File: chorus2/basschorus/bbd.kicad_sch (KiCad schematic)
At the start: 16 parts, among them J1 AVR-ISP-6, U2 ATtiny25-20S

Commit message: code implementation
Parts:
- removed C13, C14: 1u, symbol Device:C_Polarized_US
- removed R5: 10k, symbol Device:R
- added C30: 100n, symbol Device:C
- added Q1: 2N3904, Package_TO_SOT_THT:TO-92_Inline, symbol Transistor_BJT:2N3904
- added R35, R36: 180, symbol Device:R
- added R37: 3.3k, symbol Device:R
- added R38: 2.2k, symbol Device:R
- RV1: value B100K_DEPTH -> B100K_WIDTH
- RV2: value B100K_WIDTH -> B100K_DEPTH
- renumbered C8 to C12, C10 to C13, C2 to C14, C3 to C15, C6 to C9, J1 to J4, R4 to R16, R3 to R17, U2 to U7, U1 to U8
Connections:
- net +5V: now also RV1.1, R36.1, R37.1; no longer RV1.3
- net GND: now also RV1.3, R35.2, R38.2; no longer RV1.1
- new net: C30.2, Q1.2 (B), R37.2, R38.1
- new net: Q1.1 (E), R35.1
- new net: Q1.3 (C), R36.2
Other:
- note added: "3.2V -> (5-3.2)/10mA => Re=180 Gain ~= 1 => Rc=Re"
- note added: "DC offset TODO: an opamp would be worthwhile here... should be possible to add DC offset to AA filter (based on datasheet)"
- note added: "NOTE: inverted pot (clockwise = more freq = less period)"
- moved on the sheet: RV1

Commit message: fix logic
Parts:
- removed C30: 100n, symbol Device:C
- removed Q1: 2N3904, Package_TO_SOT_THT:TO-92_Inline, symbol Transistor_BJT:2N3904
- removed R35, R36: 180, symbol Device:R
- removed R37: 3.3k, symbol Device:R
- removed R38: 2.2k, symbol Device:R
- added D2: LED, symbol Device:LED
- added R15: 1k, symbol Device:R
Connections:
- net +5V: now also R15.1
- net at J4.3 (SCK), U7.7 (PB2): now also D2.1 (K); no longer RV1.2
- net at U7.2 (XTAL1/PB3): now also RV2.2
- net at U7.3 (XTAL2/PB4): now also RV1.2; no longer RV2.2
- new net: D2.2 (A), R15.2
- no-connect marks 1 -> 0
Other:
- note removed: "3.2V -> (5-3.2)/10mA => Re=180 Gain ~= 1 => Rc=Re"
- moved on the sheet: RV1, RV2

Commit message: transfer function
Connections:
- net +5V: now also RV1.3; no longer RV1.1
- net GND: now also RV1.1; no longer RV1.3
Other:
- note removed: "NOTE: inverted pot (clockwise = more freq = less period)"
- moved on the sheet: RV1
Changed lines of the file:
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@@
 		)
 	)
-	(text "NOTE: inverted pot\n(clockwise = more freq = less period)"
-		(exclude_from_sim no)
-		(at 172.72 156.21 0)
-		(effects
-			(font
-				(size 1.27 1.27)
-			)
-		)
-	)
 	(junction
 		(at 162.56 72.39)
@@
 	(symbol
 		(lib_id "Device:R_Potentiometer")
-		(at 157.48 147.32 0)
-		(mirror y)
+		(at 157.48 147.32 180)
 		(unit 1)
 		(exclude_from_sim no)
@@
 		(dnp no)
 		(property "Reference" "RV1"
-			(at 160.02 148.5901 0)
+			(at 160.02 146.0499 0)
 			(effects
 				(font
@@
 		)
 		(property "Value" "B100K_WIDTH"
-			(at 160.02 146.0501 0)
+			(at 160.02 148.5899 0)
 			(effects
 				(font

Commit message: update filters
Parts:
- renumbered C9 to C11, R15 to R16, R16 to R17, R17 to R18, RV2 to RV1, RV1 to RV2
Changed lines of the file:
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@@
 		(dnp no)
 		(fields_autoplaced yes)
-		(property "Reference" "#PWR042"
+		(property "Reference" "#PWR047"
 			(at 259.08 73.66 0)
 			(effects
@@
 			(project "basschorus"
 				(path "/7f3b4bac-3b2a-4af0-92ae-ccc3fcedc393/6358d57b-3820-48b6-8dc6-10ef393466f2"
-					(reference "#PWR042")
+					(reference "#PWR047")
 					(unit 1)
 				)
@@
 		(dnp no)
 		(fields_autoplaced yes)
-		(property "Reference" "#PWR023"
+		(property "Reference" "#PWR030"
 			(at 57.15 68.58 0)
 			(effects
@@
 			(project "basschorus"
 				(path "/7f3b4bac-3b2a-4af0-92ae-ccc3fcedc393/6358d57b-3820-48b6-8dc6-10ef393466f2"
-					(reference "#PWR023")
+					(reference "#PWR030")
 					(unit 1)
 				)
@@
 		(dnp no)
 		(fields_autoplaced yes)
-		(property "Reference" "#PWR041"
+		(property "Reference" "#PWR046"
 			(at 242.57 92.71 0)
 			(effects
@@
 			(project "basschorus"
 				(path "/7f3b4bac-3b2a-4af0-92ae-ccc3fcedc393/6358d57b-3820-48b6-8dc6-10ef393466f2"
-					(reference "#PWR041")
+					(reference "#PWR046")
 					(unit 1)
 				)
@@
 		(dnp no)
 		(fields_autoplaced yes)
-		(property "Reference" "#PWR035"
+		(property "Reference" "#PWR040"
 			(at 157.48 160.02 0)
 			(effects
@@
 			(project "basschorus"
 				(path "/7f3b4bac-3b2a-4af0-92ae-ccc3fcedc393/6358d57b-3820-48b6-8dc6-10ef393466f2"
-					(reference "#PWR035")
+					(reference "#PWR040")
 					(unit 1)
 				)
@@
 		(dnp no)
 		(fields_autoplaced yes)
-		(property "Reference" "R15"
+		(property "Reference" "R16"
 			(at 120.65 39.3699 0)
 			(effects
@@
 			(project ""
 				(path "/7f3b4bac-3b2a-4af0-92ae-ccc3fcedc393/6358d57b-3820-48b6-8dc6-10ef393466f2"
-					(reference "R15")
+					(reference "R16")
 					(unit 1)
 				)
@@
 		(dnp no)
 		(fields_autoplaced yes)
-		(property "Reference" "#PWR026"
+		(property "Reference" "#PWR033"
 			(at 86.36 142.24 0)
 			(effects
@@
 			(project "basschorus"
 				(path "/7f3b4bac-3b2a-4af0-92ae-ccc3fcedc393/6358d57b-3820-48b6-8dc6-10ef393466f2"
-					(reference "#PWR026")
+					(reference "#PWR033")
 					(unit 1)
 				)
@@
 		(dnp no)
 		(fields_autoplaced yes)
-		(property "Reference" "#PWR037"
+		(property "Reference" "#PWR042"
 			(at 173.99 93.98 0)
 			(effects
@@
 			(project "basschorus"
 				(path "/7f3b4bac-3b2a-4af0-92ae-ccc3fcedc393/6358d57b-3820-48b6-8dc6-10ef393466f2"
-					(reference "#PWR037")
+					(reference "#PWR042")
 					(unit 1)
 				)
@@
 		(dnp no)
 		(fields_autoplaced yes)
-		(property "Reference" "#PWR024"
+		(property "Reference" "#PWR031"
 			(at 57.15 83.82 0)
 			(effects
@@
 			(project "basschorus"
 				(path "/7f3b4bac-3b2a-4af0-92ae-ccc3fcedc393/6358d57b-3820-48b6-8dc6-10ef393466f2"
-					(reference "#PWR024")
+					(reference "#PWR031")
 					(unit 1)
 				)
@@
 		(dnp no)
 		(fields_autoplaced yes)
-		(property "Reference" "#PWR027"
+		(property "Reference" "#PWR034"
 			(at 92.71 59.69 0)
 			(effects
@@
 			(project "basschorus"
 				(path "/7f3b4bac-3b2a-4af0-92ae-ccc3fcedc393/6358d57b-3820-48b6-8dc6-10ef393466f2"
-					(reference "#PWR027")
+					(reference "#PWR034")
 					(unit 1)
 				)
@@
 		(dnp no)
 		(fields_autoplaced yes)
-		(property "Reference" "R17"
+		(property "Reference" "R18"
 			(at 245.11 77.4699 0)
 			(effects
@@
 			(project "basschorus"
 				(path "/7f3b4bac-3b2a-4af0-92ae-ccc3fcedc393/6358d57b-3820-48b6-8dc6-10ef393466f2"
-					(reference "R17")
+					(reference "R18")
 					(unit 1)
 				)
@@
 		(dnp no)
 		(fields_autoplaced yes)
-		(property "Reference" "#PWR038"
+		(property "Reference" "#PWR043"
 			(at 181.61 93.98 0)
 			(effects
@@
 			(project "basschorus"
 				(path "/7f3b4bac-3b2a-4af0-92ae-ccc3fcedc393/6358d57b-3820-48b6-8dc6-10ef393466f2"
-					(reference "#PWR038")
+					(reference "#PWR043")
 					(unit 1)
 				)
@@
 		(dnp no)
 		(fields_autoplaced yes)
-		(property "Reference" "#PWR029"
+		(property "Reference" "#PWR036"
 			(at 118.11 38.1 0)
 			(effects
@@
 			(project "basschorus"
 				(path "/7f3b4bac-3b2a-4af0-92ae-ccc3fcedc393/6358d57b-3820-48b6-8dc6-10ef393466f2"
-					(reference "#PWR029")
+					(reference "#PWR036")
 					(unit 1)
 				)
@@
 		(dnp no)
 		(fields_autoplaced yes)
-		(property "Reference" "#PWR040"
+		(property "Reference" "#PWR045"
 			(at 204.47 95.25 0)
 			(effects
@@
 			(project "basschorus"
 				(path "/7f3b4bac-3b2a-4af0-92ae-ccc3fcedc393/6358d57b-3820-48b6-8dc6-10ef393466f2"
-					(reference "#PWR040")
+					(reference "#PWR045")
 					(unit 1)
 				)
@@
 		(dnp no)
 		(fields_autoplaced yes)
-		(property "Reference" "#PWR039"
+		(property "Reference" "#PWR044"
 			(at 204.47 62.23 0)
 			(effects
@@
 			(project "basschorus"
 				(path "/7f3b4bac-3b2a-4af0-92ae-ccc3fcedc393/6358d57b-3820-48b6-8dc6-10ef393466f2"
-					(reference "#PWR039")
+					(reference "#PWR044")
 					(unit 1)
 				)
@@
 		(on_board yes)
 		(dnp no)
-		(property "Reference" "RV1"
+		(property "Reference" "RV2"
 			(at 160.02 146.0499 0)
 			(effects
@@
 			(project "basschorus"
 				(path "/7f3b4bac-3b2a-4af0-92ae-ccc3fcedc393/6358d57b-3820-48b6-8dc6-10ef393466f2"
-					(reference "RV1")
+					(reference "RV2")
 					(unit 1)
 				)
@@
 		(dnp no)
 		(fields_autoplaced yes)
-		(property "Reference" "#PWR036"
+		(property "Reference" "#PWR041"
 			(at 162.56 91.44 0)
 			(effects
@@
 			(project "basschorus"
 				(path "/7f3b4bac-3b2a-4af0-92ae-ccc3fcedc393/6358d57b-3820-48b6-8dc6-10ef393466f2"
-					(reference "#PWR036")
+					(reference "#PWR041")
 					(unit 1)
 				)
@@
 		(dnp no)
 		(fields_autoplaced yes)
-		(property "Reference" "C9"
+		(property "Reference" "C11"
 			(at 60.96 69.8499 0)
 			(effects
@@
 			(project "basschorus"
 				(path "/7f3b4bac-3b2a-4af0-92ae-ccc3fcedc393/6358d57b-3820-48b6-8dc6-10ef393466f2"
-					(reference "C9")
+					(reference "C11")
 					(unit 1)
 				)
@@
 		(dnp no)
 		(fields_autoplaced yes)
-		(property "Reference" "#PWR025"
+		(property "Reference" "#PWR032"
 			(at 86.36 110.49 0)
 			(effects
@@
 			(project "basschorus"
 				(path "/7f3b4bac-3b2a-4af0-92ae-ccc3fcedc393/6358d57b-3820-48b6-8dc6-10ef393466f2"
-					(reference "#PWR025")
+					(reference "#PWR032")
 					(unit 1)
 				)
@@
 		(dnp no)
 		(fields_autoplaced yes)
-		(property "Reference" "R16"
+		(property "Reference" "R17"
 			(at 156.21 66.04 90)
 			(effects
@@
 			(project "basschorus"
 				(path "/7f3b4bac-3b2a-4af0-92ae-ccc3fcedc393/6358d57b-3820-48b6-8dc6-10ef393466f2"
-					(reference "R16")
+					(reference "R17")
 					(unit 1)
 				)
@@
 		(dnp no)
 		(fields_autoplaced yes)
-		(property "Reference" "#PWR034"
+		(property "Reference" "#PWR039"
 			(at 157.48 144.78 0)
 			(effects
@@
 			(project "basschorus"
 				(path "/7f3b4bac-3b2a-4af0-92ae-ccc3fcedc393/6358d57b-3820-48b6-8dc6-10ef393466f2"
-					(reference "#PWR034")
+					(reference "#PWR039")
 					(unit 1)
 				)
@@
 		(dnp no)
 		(fields_autoplaced yes)
-		(property "Reference" "#PWR043"
+		(property "Reference" "#PWR048"
 			(at 259.08 88.9 0)
 			(effects
@@
 			(project "basschorus"
 				(path "/7f3b4bac-3b2a-4af0-92ae-ccc3fcedc393/6358d57b-3820-48b6-8dc6-10ef393466f2"
-					(reference "#PWR043")
+					(reference "#PWR048")
 					(unit 1)
 				)
@@
 		(on_board yes)
 		(dnp no)
-		(property "Reference" "RV2"
+		(property "Reference" "RV1"
 			(at 149.86 121.9199 0)
 			(effects
@@
 			(project "basschorus"
 				(path "/7f3b4bac-3b2a-4af0-92ae-ccc3fcedc393/6358d57b-3820-48b6-8dc6-10ef393466f2"
-					(reference "RV2")
+					(reference "RV1")
 					(unit 1)
 				)
@@
 		(dnp no)
 		(fields_autoplaced yes)
-		(property "Reference" "#PWR031"
+		(property "Reference" "#PWR037"
 			(at 147.32 120.65 0)
 			(effects
@@
 			(project "basschorus"
 				(path "/7f3b4bac-3b2a-4af0-92ae-ccc3fcedc393/6358d57b-3820-48b6-8dc6-10ef393466f2"
-					(reference "#PWR031")
+					(reference "#PWR037")
 					(unit 1)
 				)
@@
 		(dnp no)
 		(fields_autoplaced yes)
-		(property "Reference" "#PWR028"
+		(property "Reference" "#PWR035"
 			(at 92.71 100.33 0)
 			(effects
@@
 			(project "basschorus"
 				(path "/7f3b4bac-3b2a-4af0-92ae-ccc3fcedc393/6358d57b-3820-48b6-8dc6-10ef393466f2"
-					(reference "#PWR028")
+					(reference "#PWR035")
 					(unit 1)
 				)
@@
 		(dnp no)
 		(fields_autoplaced yes)
-		(property "Reference" "#PWR032"
+		(property "Reference" "#PWR038"
 			(at 147.32 135.89 0)
 			(effects
@@
 			(project "basschorus"
 				(path "/7f3b4bac-3b2a-4af0-92ae-ccc3fcedc393/6358d57b-3820-48b6-8dc6-10ef393466f2"
-					(reference "#PWR032")
-					(unit 1)
-				)
+					(reference "#PWR038")
+					(unit 1)
+				)

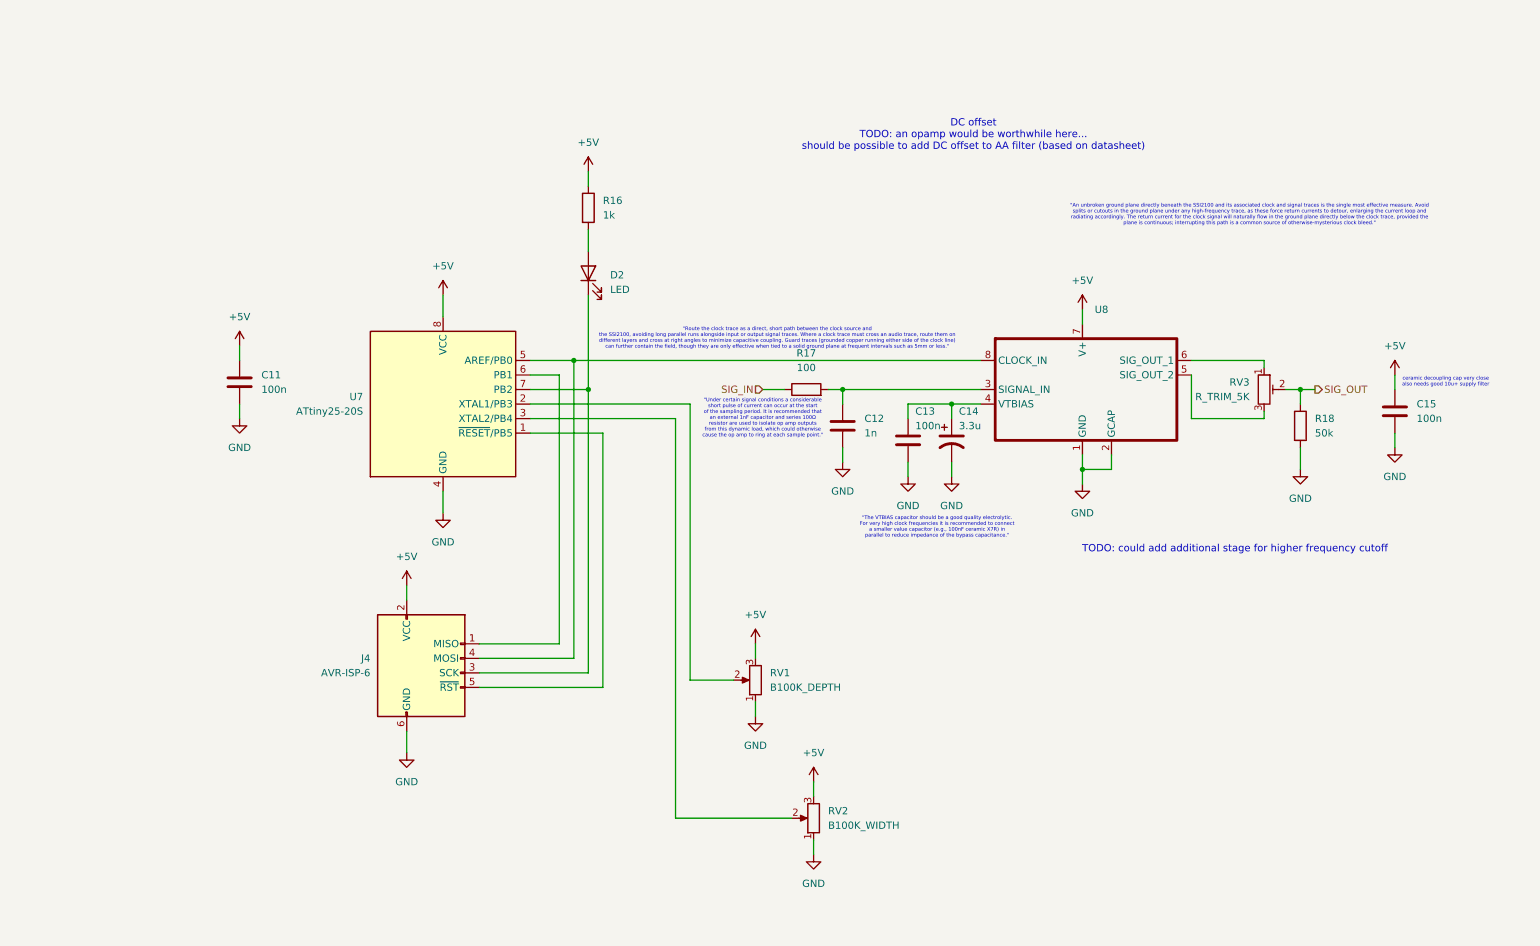
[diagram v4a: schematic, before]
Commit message: update designs based on new calculations
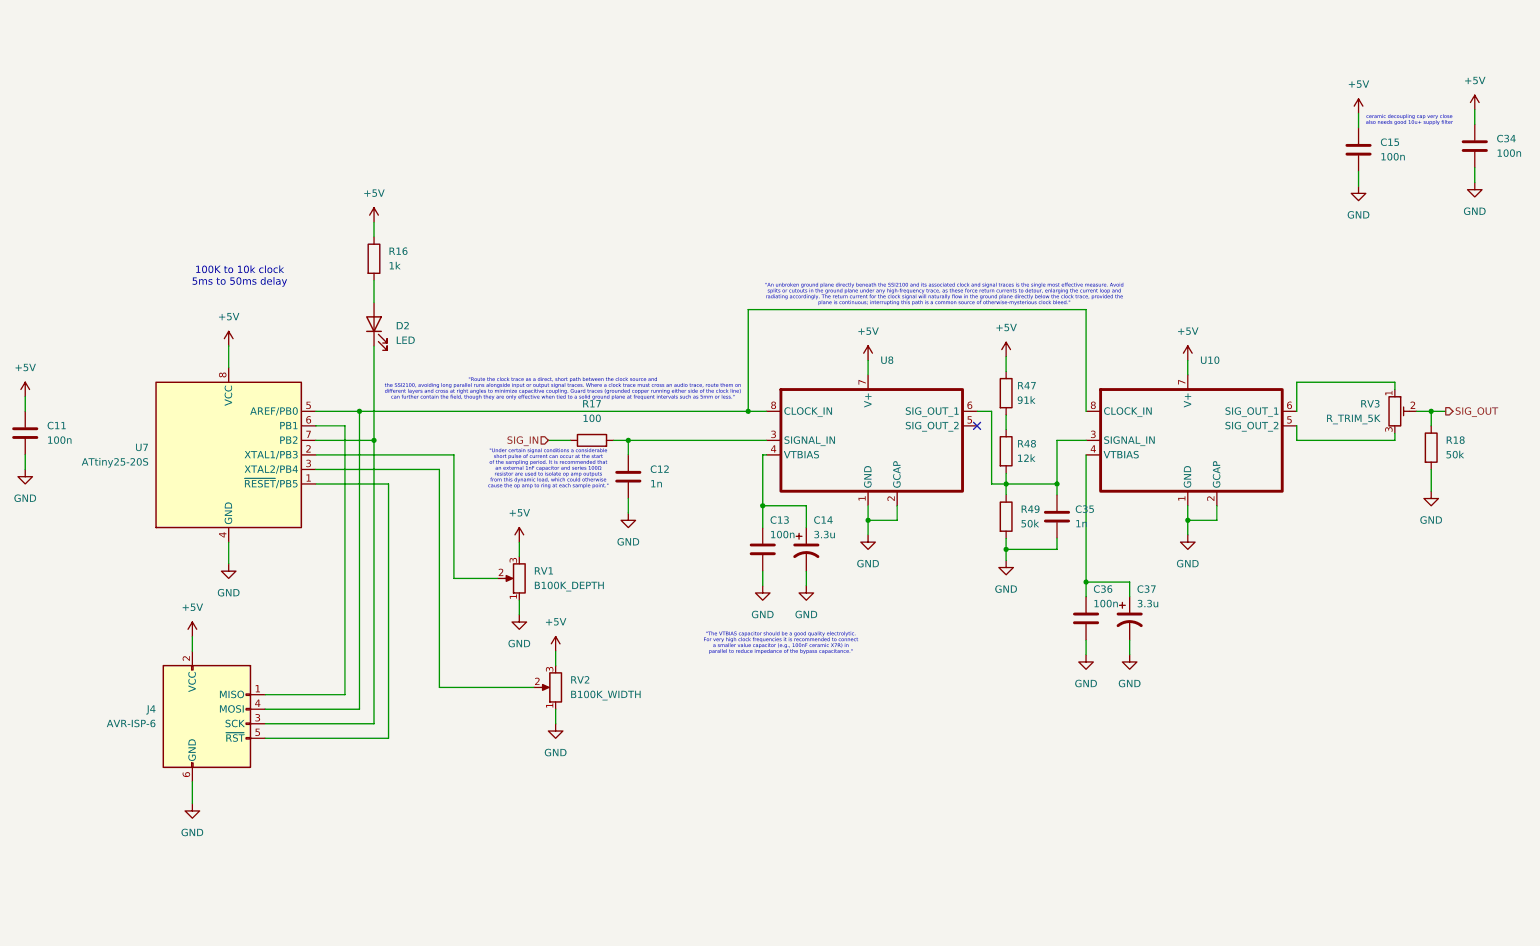
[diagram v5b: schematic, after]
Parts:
- added C34, C36: 100n, symbol Device:C
- added C35: 1n, symbol Device:C
- added C37: 3.3u, symbol Device:C_Polarized_US
- added R47: 91k, symbol Device:R
- added R48: 12k, symbol Device:R
- added R49: 50k, symbol Device:R
- added U10: ~, Package_SO:SOP-8_3.76x4.96mm_P1.27mm, symbol _project:SSI2100
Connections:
- net +5V: now also C34.1, R47.1, U10.7 (V+)
- net GND: now also C34.2, C35.2, C36.2, C37.2, R49.2, U10.1 (GND), U10.2 (GCAP)
- net at RV3.1: now also U10.6 (SIG_OUT_1); no longer U8.6 (SIG_OUT_1)
- net at RV3.3: now also U10.5 (SIG_OUT_2); no longer U8.5 (SIG_OUT_2)
- net at J4.4 (MOSI), U7.5 (AREF/PB0), U8.8 (CLOCK_IN): now also U10.8 (CLOCK_IN)
- new net: C35.1, R48.2, R49.1, U10.3 (SIGNAL_IN), U8.6 (SIG_OUT_1)
- new net: C36.1, C37.1, U10.4 (VTBIAS)
- new net: R47.2, R48.1
- no-connect marks 0 -> 1
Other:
- note added: "100K to 10k clock 5ms to 50ms delay"
- note removed: "DC offset TODO: an opamp would be worthwhile here... should be possible to add DC offset to AA filter (based on datasheet)"
- note removed: "TODO: could add additional stage for higher frequency cutoff"
- moved on the sheet: C11, C12, C13, C14, C15, D2, J4, R16, R17, R18, RV1, RV2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

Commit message: assign parts for testing
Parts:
- added TP13, TP14: TestPoint, TestPoint:TestPoint_THTPad_2.5x2.5mm_Drill1.2mm, symbol Connector:TestPoint
- C12: renamed from C11; footprint (none) -> Capacitor_THT:C_Rect_L7.0mm_W2.5mm_P5.00mm
- C13: renamed from C12; footprint (none) -> Capacitor_THT:C_Rect_L7.0mm_W2.5mm_P5.00mm
- C14: renamed from C13; footprint (none) -> Capacitor_THT:C_Rect_L7.0mm_W2.5mm_P5.00mm
- C15: renamed from C14; footprint (none) -> Capacitor_THT:CP_Radial_D8.0mm_P5.00mm
- C16: renamed from C35; footprint (none) -> Capacitor_THT:C_Rect_L7.0mm_W2.5mm_P5.00mm
- C17: renamed from C36; footprint (none) -> Capacitor_THT:C_Rect_L7.0mm_W2.5mm_P5.00mm
- C18: renamed from C37; footprint (none) -> Capacitor_THT:CP_Radial_D8.0mm_P5.00mm
- C19: renamed from C15; footprint (none) -> Capacitor_THT:C_Rect_L7.0mm_W2.5mm_P5.00mm
- C20: renamed from C34; footprint (none) -> Capacitor_THT:C_Rect_L7.0mm_W2.5mm_P5.00mm
- D2: footprint (none) -> LED_THT:LED_Rectangular_W5.0mm_H2.0mm
- J4: footprint (none) -> Connector_PinHeader_2.54mm:PinHeader_2x03_P2.54mm_Vertical
- R16, R17: footprint (none) -> Resistor_THT:R_Axial_DIN0204_L3.6mm_D1.6mm_P5.08mm_Horizontal
- R18: renamed from R47; footprint (none) -> Resistor_THT:R_Axial_DIN0204_L3.6mm_D1.6mm_P5.08mm_Horizontal
- R19: renamed from R48; footprint (none) -> Resistor_THT:R_Axial_DIN0204_L3.6mm_D1.6mm_P5.08mm_Horizontal
- R20: renamed from R49; footprint (none) -> Resistor_THT:R_Axial_DIN0204_L3.6mm_D1.6mm_P5.08mm_Horizontal
- R21: renamed from R18; footprint (none) -> Resistor_THT:R_Axial_DIN0204_L3.6mm_D1.6mm_P5.08mm_Horizontal
- RV3: renamed from RV1; footprint (none) -> Potentiometer_THT:Potentiometer_Alpha_RD901F-40-00D_Single_Vertical_CircularHoles
- RV4: renamed from RV2; footprint (none) -> Potentiometer_THT:Potentiometer_Alpha_RD901F-40-00D_Single_Vertical_CircularHoles
- RV5: renamed from RV3; footprint (none) -> Potentiometer_THT:Potentiometer_Vishay_T73YP_Vertical
- U8: renamed from U7; footprint Package_SO:SOIC-8_5.3x5.3mm_P1.27mm -> Package_DIP:DIP-8_W7.62mm
- renumbered U8 to U9
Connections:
- net at C16.1, R19.2, R20.1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: now also TP14.1
- net at J4.4 (MOSI), U10.8 (CLOCK_IN), U8.5 (AREF/PB0)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: now also TP13.1

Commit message: started layout
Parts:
- TP13: value TestPoint -> CLK
- TP14: value TestPoint -> BBD1
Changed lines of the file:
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@@
 			)
 		)
-		(property "Value" "TestPoint"
+		(property "Value" "BBD1"
 			(at 185.293 86.36 90)
 			(effects
@@
 		(fields_autoplaced yes)
 		(property "Reference" "TP13"
-			(at 75.565 71.6279 0)
+			(at 76.2 71.6279 0)
 			(effects
 				(font
@@
 			)
 		)
-		(property "Value" "TestPoint"
-			(at 75.565 74.1679 0)
-			(effects
-				(font
+		(property "Value" "CLK"
+			(at 76.2 74.1679 0)
+			(effects
+				(font

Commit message: basic layout
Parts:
- R16, R17, R18, R19, R20, R21: footprint Resistor_THT:R_Axial_DIN0204_L3.6mm_D1.6mm_P5.08mm_Horizontal -> Resistor_THT:R_Axial_DIN0204_L3.6mm_D1.6mm_P2.54mm_Vertical
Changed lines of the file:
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@@
 			)
 		)
-		(property "Footprint" "Resistor_THT:R_Axial_DIN0204_L3.6mm_D1.6mm_P5.08mm_Horizontal"
+		(property "Footprint" "Resistor_THT:R_Axial_DIN0204_L3.6mm_D1.6mm_P2.54mm_Vertical"
 			(at 189.357 94.615 90)
 			(effects
@@
 			)
 		)
-		(property "Footprint" "Resistor_THT:R_Axial_DIN0204_L3.6mm_D1.6mm_P5.08mm_Horizontal"
+		(property "Footprint" "Resistor_THT:R_Axial_DIN0204_L3.6mm_D1.6mm_P2.54mm_Vertical"
 			(at 78.867 49.53 90)
 			(effects
@@
 			)
 		)
-		(property "Footprint" "Resistor_THT:R_Axial_DIN0204_L3.6mm_D1.6mm_P5.08mm_Horizontal"
+		(property "Footprint" "Resistor_THT:R_Axial_DIN0204_L3.6mm_D1.6mm_P2.54mm_Vertical"
 			(at 263.652 82.55 90)
 			(effects
@@
 			)
 		)
-		(property "Footprint" "Resistor_THT:R_Axial_DIN0204_L3.6mm_D1.6mm_P5.08mm_Horizontal"
+		(property "Footprint" "Resistor_THT:R_Axial_DIN0204_L3.6mm_D1.6mm_P2.54mm_Vertical"
 			(at 189.357 73.025 90)
 			(effects
@@
 			)
 		)
-		(property "Footprint" "Resistor_THT:R_Axial_DIN0204_L3.6mm_D1.6mm_P5.08mm_Horizontal"
+		(property "Footprint" "Resistor_THT:R_Axial_DIN0204_L3.6mm_D1.6mm_P2.54mm_Vertical"
 			(at 118.745 83.058 90)
 			(effects
@@
 			)
 		)
-		(property "Footprint" "Resistor_THT:R_Axial_DIN0204_L3.6mm_D1.6mm_P5.08mm_Horizontal"
+		(property "Footprint" "Resistor_THT:R_Axial_DIN0204_L3.6mm_D1.6mm_P2.54mm_Vertical"
 			(at 189.357 83.185 90)
 			(effects
